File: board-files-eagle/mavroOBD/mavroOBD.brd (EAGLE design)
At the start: 42 x 20 mm, 27 parts, among them Q1 8mhz / 490-1198-1-ND, Q2 16mhz / 490-1198-1-ND, U1 ATMEGA328, U3 MCP2551, U4 MCP2515

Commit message: Fixed Tag Connect ISP pin assignments
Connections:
- net CS: no longer J1.4
- net D9: no longer J1.3
- net MISO: now also J1.1
- net MOSI: now also J1.4; no longer J1.1
- net SCK: now also J1.3
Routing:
- net CS: track 15.6 -> 7.28 mm
- net D9: track 16.0 -> 11.7 mm
- net MISO: track 10.0 -> 13.1 mm
- net SCK: track 15.2 -> 12.7 mm
- net MOSI: track 13.4 -> 11.0 mm, vias 2 -> 0
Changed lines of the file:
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@@
 <contactref element="U1" pad="17"/>
 <contactref element="U4" pad="13"/>
-<wire x1="18.6351" y1="14.78" x2="15.34" y2="14.78" width="0.2032" layer="1"/>
-<wire x1="15.34" y1="14.78" x2="15.2" y2="14.64" width="0.2032" layer="1"/>
-<via x="15.2" y="14.64" extent="1-16" drill="0.5" shape="octagon"/>
-<via x="9.6" y="15.8" extent="1-16" drill="0.5" shape="octagon"/>
-<wire x1="9.6" y1="15.8" x2="9.6" y2="14.670653125" width="0.2032" layer="1"/>
-<wire x1="9.6" y1="14.670653125" x2="9.444571875" y2="14.515225" width="0.2032" layer="1"/>
-<wire x1="9.6" y1="15.8" x2="9.6" y2="18.6" width="0.2032" layer="16"/>
-<wire x1="9.6" y1="18.6" x2="10" y2="19" width="0.2032" layer="16"/>
-<wire x1="10" y1="19" x2="10.84" y2="19" width="0.2032" layer="16"/>
-<wire x1="10.84" y1="19" x2="15.2" y2="14.64" width="0.2032" layer="16"/>
+<contactref element="J1" pad="3"/>
+<wire x1="18.6351" y1="14.78" x2="15.395" y2="14.78" width="0.2032" layer="1"/>
+<wire x1="15.395" y1="14.78" x2="14.5875" y2="15.5875" width="0.2032" layer="1"/>
+<wire x1="14.5875" y1="15.5875" x2="13.42" y2="16.755" width="0.2032" layer="1"/>
+<wire x1="9.444571875" y1="14.515225" x2="9.444571875" y2="15.634571875" width="0.2032" layer="1"/>
+<wire x1="9.444571875" y1="15.634571875" x2="9.65" y2="15.84" width="0.2032" layer="1"/>
+<via x="9.65" y="15.84" extent="1-16" drill="0.5" diameter="1.008" shape="octagon"/>
+<wire x1="9.65" y1="15.84" x2="13.38" y2="15.84" width="0.2032" layer="16"/>
+<wire x1="13.38" y1="15.84" x2="13.62" y2="15.42" width="0.2032" layer="16"/>
+<via x="13.62" y="15.42" extent="1-16" drill="0.5" diameter="1.008" shape="octagon"/>
+<wire x1="13.62" y1="15.42" x2="14.42" y2="15.42" width="0.2032" layer="1"/>
+<wire x1="14.42" y1="15.42" x2="14.5875" y2="15.5875" width="0.2032" layer="1"/>
 </signal>
 <signal name="MISO">
@@
 <wire x1="10.71" y1="13.15" x2="10.71" y2="13.6698" width="0.2032" layer="1"/>
 <wire x1="10.71" y1="13.6698" x2="11.555425" y2="14.515225" width="0.2032" layer="1"/>
+<contactref element="J1" pad="1"/>
+<wire x1="12.15" y1="16.755" x2="11.715" y2="16.755" width="0.2032" layer="1"/>
+<wire x1="11.715" y1="16.755" x2="11.09" y2="16.13" width="0.2032" layer="1"/>
+<wire x1="11.09" y1="16.13" x2="11.09" y2="14.98065" width="0.2032" layer="1"/>
+<wire x1="11.09" y1="14.98065" x2="11.555425" y2="14.515225" width="0.2032" layer="1"/>
 </signal>
 <signal name="MOSI">
 <contactref element="U1" pad="15"/>
 <contactref element="U4" pad="14"/>
-<contactref element="J1" pad="1"/>
-<wire x1="12.15" y1="16.755" x2="12.15" y2="16.24" width="0.2032" layer="1"/>
-<wire x1="12.15" y1="16.24" x2="12.15" y2="16.15" width="0.2032" layer="1"/>
-<wire x1="12.15" y1="16.15" x2="12.72" y2="15.58" width="0.2032" layer="1"/>
-<wire x1="12.72" y1="15.58" x2="12.72" y2="14.548425" width="0.2032" layer="1"/>
+<contactref element="J1" pad="4"/>
+<wire x1="13.42" y1="18.025" x2="13.42" y2="17.97" width="0.2032" layer="1"/>
+<wire x1="12.8" y1="17.405" x2="12.8" y2="14.548425" width="0.2032" layer="1"/>
+<wire x1="12.8" y1="17.405" x2="13.42" y2="18.025" width="0.2032" layer="1"/>
+<wire x1="12.8" y1="14.548425" x2="12.72" y2="14.548425" width="0.2032" layer="1"/>
 <wire x1="12.72" y1="14.548425" x2="12.1211125" y2="13.9495375" width="0.2032" layer="1"/>
-<wire x1="18.6351" y1="13.51" x2="16" y2="13.51" width="0.2032" layer="1"/>
-<via x="16" y="13.51" extent="1-16" drill="0.5" shape="octagon"/>
-<via x="11.02" y="15.59" extent="1-16" drill="0.5" shape="octagon"/>
-<wire x1="11.02" y1="15.59" x2="11.23" y2="15.32" width="0.2032" layer="1"/>
-<wire x1="11.23" y1="15.32" x2="12.15" y2="16.24" width="0.2032" layer="1"/>
-<wire x1="16" y1="13.51" x2="14.79" y2="13.51" width="0.2032" layer="16"/>
-<wire x1="14.79" y1="13.51" x2="12.72" y2="15.58" width="0.2032" layer="16"/>
-<wire x1="12.72" y1="15.58" x2="11.03" y2="15.58" width="0.2032" layer="16"/>
-<wire x1="11.03" y1="15.58" x2="11.02" y2="15.59" width="0.2032" layer="16"/>
+<wire x1="12.8" y1="14.548425" x2="14.171575" y2="14.548425" width="0.2032" layer="1"/>
+<wire x1="14.171575" y1="14.548425" x2="15.19" y2="13.53" width="0.2032" layer="1"/>
+<wire x1="15.19" y1="13.53" x2="18.6151" y2="13.53" width="0.2032" layer="1"/>
+<wire x1="18.6151" y1="13.53" x2="18.6351" y2="13.51" width="0.2032" layer="1"/>
 </signal>
 <signal name="N$7">
@@
 <contactref element="U1" pad="13"/>
 <contactref element="R6" pad="1"/>
-<contactref element="J1" pad="3"/>
-<wire x1="13.42" y1="16.755" x2="13.42" y2="16.43" width="0.2032" layer="1"/>
-<wire x1="13.42" y1="16.43" x2="13.87" y2="15.91" width="0.2032" layer="1"/>
-<wire x1="13.87" y1="15.91" x2="13.87" y2="13.4356875" width="0.2032" layer="1"/>
-<wire x1="13.87" y1="13.4356875" x2="13.25248125" y2="12.81816875" width="0.2032" layer="1"/>
 <wire x1="13.25248125" y1="12.81816875" x2="13.21816875" y2="12.81816875" width="0.2032" layer="1"/>
 <wire x1="13.21816875" y1="12.81816875" x2="12.16" y2="11.76" width="0.2032" layer="1"/>
@@
 <contactref element="U4" pad="16"/>
 <contactref element="U1" pad="14"/>
-<contactref element="J1" pad="4"/>
-<wire x1="13.42" y1="18.025" x2="13.42" y2="17.97" width="0.2032" layer="1"/>
-<wire x1="13.42" y1="17.97" x2="12.78" y2="17.4" width="0.2032" layer="1"/>
-<wire x1="12.78" y1="17.4" x2="12.78" y2="16.22" width="0.2032" layer="1"/>
-<wire x1="12.78" y1="16.22" x2="13.31" y2="15.7" width="0.2032" layer="1"/>
-<wire x1="13.31" y1="15.7" x2="13.31" y2="14.00705625" width="0.2032" layer="1"/>
-<wire x1="13.31" y1="14.00705625" x2="12.686796875" y2="13.383853125" width="0.2032" layer="1"/>
-<wire x1="18.6351" y1="10.97" x2="16.99" y2="10.97" width="0.2032" layer="1"/>
-<wire x1="16.99" y1="10.97" x2="14.45" y2="13.49" width="0.2032" layer="1"/>
-<wire x1="14.45" y1="13.49" x2="14.45" y2="16.05" width="0.2032" layer="1"/>
-<wire x1="14.45" y1="16.05" x2="14.07" y2="16.44" width="0.2032" layer="1"/>
-<wire x1="14.07" y1="16.44" x2="14.07" y2="16.94" width="0.2032" layer="1"/>
-<wire x1="14.07" y1="16.94" x2="13.63" y2="17.39" width="0.2032" layer="1"/>
-<wire x1="13.63" y1="17.39" x2="13.63" y2="17.815" width="0.2032" layer="1"/>
-<wire x1="13.63" y1="17.815" x2="13.42" y2="18.025" width="0.2032" layer="1"/>
+<wire x1="18.6351" y1="10.97" x2="16.9" y2="10.97" width="0.2032" layer="1"/>
+<wire x1="16.9" y1="10.97" x2="14.08" y2="13.79" width="0.2032" layer="1"/>
+<wire x1="14.08" y1="13.79" x2="13.09294375" y2="13.79" width="0.2032" layer="1"/>
+<wire x1="13.09294375" y1="13.79" x2="12.686796875" y2="13.383853125" width="0.2032" layer="1"/>
 </signal>
 <signal name="INT">

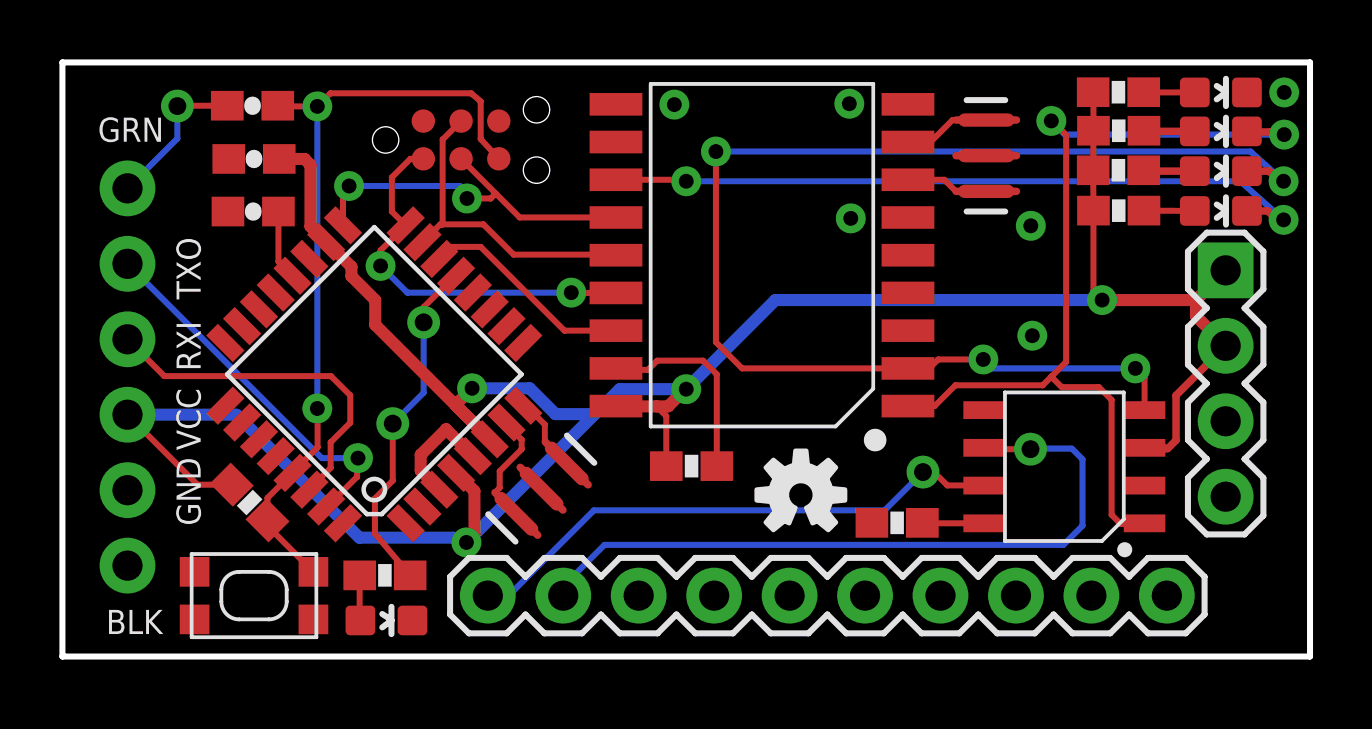
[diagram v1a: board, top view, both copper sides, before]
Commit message: REV 3 Board - Sent to OSHPark
Fixed a few via sizes, added VCC to ISP pin and REV 3 to silkscreen.
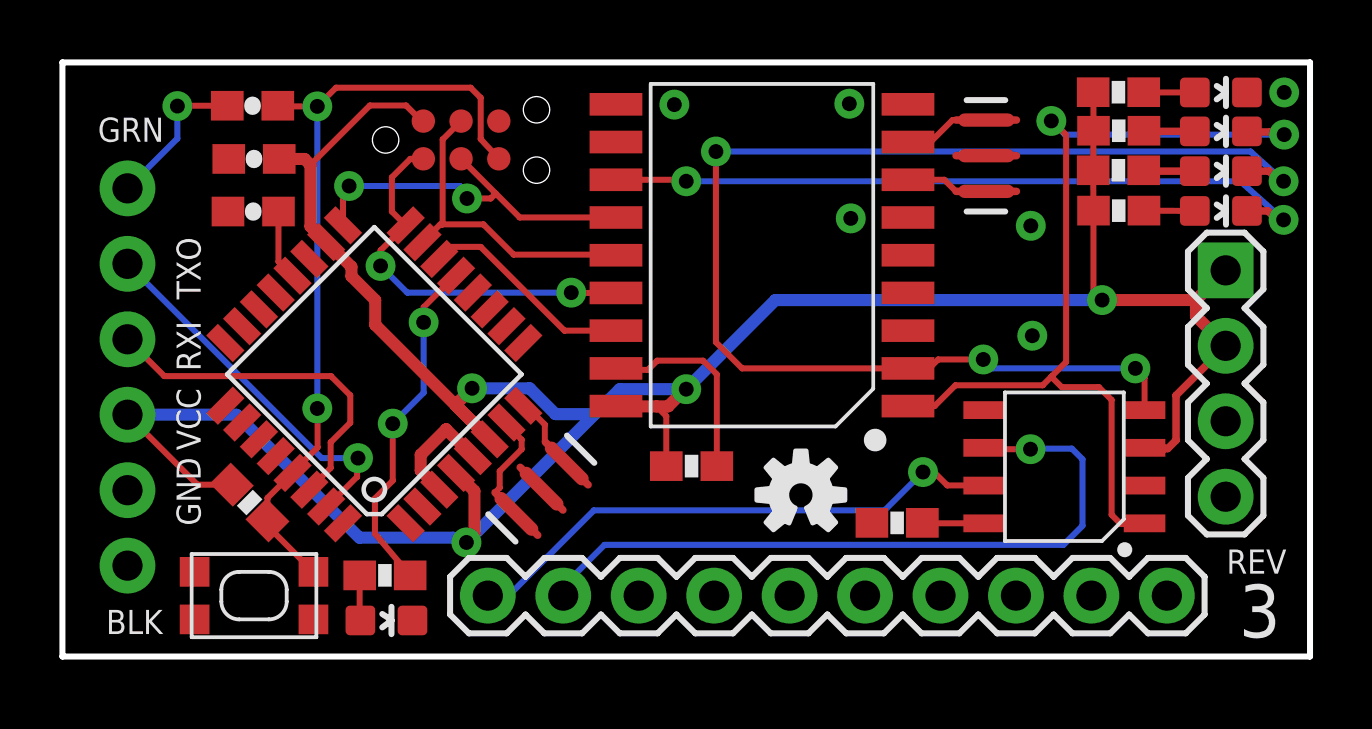
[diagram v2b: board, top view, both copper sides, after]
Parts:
- Q1: value 8mhz / 490-1198-1-ND -> 16mhz / 490-1198-1-ND
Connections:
- removed net 3.3V: J1.2
- net VCC: now also J1.2
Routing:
- net VCC: track 88.9 -> 93.7 mm
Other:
- board text added: "3"
- board text added: "REV"
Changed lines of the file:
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@@
 <text x="3.416" y="18.142" size="0.8128" layer="21" ratio="15" rot="R180">GRN</text>
 <wire x1="42" y1="0" x2="0" y2="0" width="0.2032" layer="20"/>
+<text x="41.206" y="3.602" size="0.8128" layer="21" ratio="15" rot="R180">REV</text>
+<text x="41.006" y="2.422" size="1.778" layer="21" ratio="15" rot="R180">3</text>
 </plain>
 <attributes>
@@
 <element name="C2" library="SparkFun" package="0603-CAP" value="0.1uF" x="6.4" y="18.5416" smashed="yes" rot="R180"/>
 <element name="U$3" library="SparkFun" package="OSHW-LOGO-S" value="OSHW-LOGOS" x="24.8594" y="5.4384"/>
-<element name="Q1" library="Testing" package="RESONATOR-SMD-1:1" value="8mhz / 490-1198-1-ND" x="16.13" y="5.65" smashed="yes" rot="R45"/>
+<element name="Q1" library="Testing" package="RESONATOR-SMD-1:1" value="16mhz / 490-1198-1-ND" x="16.13" y="5.65" smashed="yes" rot="R45"/>
 <element name="U3" library="IC" package="SOIC8-6.0" value="MCP2551" x="33.73" y="6.39" smashed="yes" rot="R90"/>
 <element name="U4" library="IC" package="SOIC18" value="MCP2515" x="23.55" y="13.51" smashed="yes" rot="R90"/>
@@
 <wire x1="14.69" y1="16.755" x2="14.69" y2="16.76" width="0.2032" layer="1"/>
 <wire x1="14.69" y1="16.76" x2="14.08" y2="17.42" width="0.2032" layer="1"/>
-<wire x1="14.08" y1="17.42" x2="14.08" y2="18.69" width="0.2032" layer="1"/>
-<wire x1="14.08" y1="18.69" x2="13.76" y2="18.96" width="0.2032" layer="1"/>
-<wire x1="13.76" y1="18.96" x2="9.02" y2="18.96" width="0.2032" layer="1"/>
-<wire x1="9.02" y1="18.96" x2="8.58" y2="18.52" width="0.2032" layer="1"/>
+<wire x1="14.08" y1="17.42" x2="14.08" y2="18.81" width="0.2032" layer="1"/>
+<wire x1="9.21" y1="19.15" x2="8.58" y2="18.52" width="0.2032" layer="1"/>
 <wire x1="8.58" y1="18.52" x2="8.58" y2="8.35" width="0.2032" layer="16"/>
 <wire x1="7.747515625" y1="6.181828125" x2="7.747515625" y2="6.197515625" width="0.2032" layer="1"/>
@@
 <wire x1="6.903440625" y1="4.58235625" x2="6.903440625" y2="4.396559375" width="0.2032" layer="1"/>
 <wire x1="6.903440625" y1="4.396559375" x2="8.45" y2="2.85" width="0.2032" layer="1"/>
+<wire x1="14.08" y1="18.81" x2="13.74" y2="19.15" width="0.2032" layer="1"/>
+<wire x1="13.74" y1="19.15" x2="9.21" y2="19.15" width="0.2032" layer="1"/>
 </signal>
 <signal name="SCK">
@@
 <wire x1="37.49" y1="7.28" x2="37.49" y2="8.79" width="0.254" layer="1"/>
 <wire x1="37.49" y1="8.79" x2="39.16" y2="10.46" width="0.254" layer="1"/>
+<contactref element="J1" pad="2"/>
+<wire x1="12.15" y1="18.025" x2="12.095" y2="18.025" width="0.2032" layer="1"/>
+<wire x1="12.095" y1="18.025" x2="11.57" y2="18.55" width="0.2032" layer="1"/>
+<wire x1="11.57" y1="18.55" x2="10.35" y2="18.55" width="0.2032" layer="1"/>
+<wire x1="10.35" y1="18.55" x2="8.35" y2="16.55" width="0.2032" layer="1"/>
 </signal>
 <signal name="D9">
@@
 <wire x1="13.21816875" y1="12.81816875" x2="12.16" y2="11.76" width="0.2032" layer="1"/>
 <wire x1="12.16" y1="11.76" x2="12.16" y2="11.25" width="0.2032" layer="1"/>
-<via x="12.16" y="11.25" extent="1-16" drill="0.6" shape="octagon"/>
+<via x="12.16" y="11.25" extent="1-16" drill="0.5" shape="octagon"/>
 <wire x1="12.16" y1="11.25" x2="12.16" y2="8.88" width="0.2032" layer="16"/>
 <wire x1="12.16" y1="8.88" x2="11.12" y2="7.84" width="0.2032" layer="16"/>
-<via x="11.12" y="7.84" extent="1-16" drill="0.6" shape="octagon"/>
+<via x="11.12" y="7.84" extent="1-16" drill="0.5"/>
 <wire x1="11.12" y1="7.84" x2="11.12" y2="5.92" width="0.2032" layer="1"/>
 <wire x1="11.12" y1="5.92" x2="10.52" y2="5.32" width="0.2032" layer="1"/>
@@
 <wire x1="5.55" y1="18.5416" x2="3.8816" y2="18.5416" width="0.2032" layer="1"/>
 <wire x1="3.8816" y1="18.5416" x2="3.87" y2="18.53" width="0.2032" layer="1"/>
-<via x="3.87" y="18.53" extent="1-16" drill="0.6" shape="octagon"/>
+<via x="3.87" y="18.53" extent="1-16" drill="0.5" shape="octagon"/>
 <wire x1="3.87" y1="18.53" x2="3.87" y2="17.44" width="0.2032" layer="16"/>
 <wire x1="3.87" y1="17.44" x2="2.19" y2="15.76" width="0.2032" layer="16"/>
@@
 <wire x1="17.89" y1="4.92" x2="27.68" y2="4.92" width="0.2032" layer="16"/>
 <wire x1="27.68" y1="4.92" x2="28.97" y2="6.21" width="0.2032" layer="16"/>
-<via x="28.97" y="6.21" extent="1-16" drill="0.6" shape="octagon"/>
+<via x="28.97" y="6.21" extent="1-16" drill="0.5"/>
 <wire x1="28.97" y1="6.21" x2="29.34" y2="6.21" width="0.2032" layer="1"/>
 <wire x1="29.34" y1="6.21" x2="29.79" y2="5.76" width="0.2032" layer="1"/>
@@
 <wire x1="33.98" y1="7" x2="32.61" y2="7" width="0.2032" layer="16"/>
 <wire x1="32.61" y1="7" x2="32.59" y2="6.98" width="0.2032" layer="16"/>
-<via x="32.59" y="6.98" extent="1-16" drill="0.6" shape="octagon"/>
+<via x="32.59" y="6.98" extent="1-16" drill="0.5" shape="octagon"/>
 <wire x1="32.59" y1="6.98" x2="31.075" y2="6.98" width="0.2032" layer="1"/>
 <wire x1="31.075" y1="6.98" x2="31.03" y2="7.025" width="0.2032" layer="1"/>
@@
 <wire x1="36.408" y1="18.99" x2="36.4" y2="18.998" width="0.2032" layer="1"/>
 </signal>
-<signal name="3.3V" class="1">
-<contactref element="J1" pad="2"/>
-</signal>
 </signals>
